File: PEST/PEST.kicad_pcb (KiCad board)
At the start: 4 copper layers, 6.2 x 4.9 mm, 4 parts, among them J1 Conn_01x01, J2 Conn_01x01, J3 Conn_01x01, J4 Conn_01x01

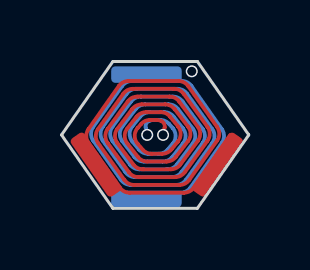
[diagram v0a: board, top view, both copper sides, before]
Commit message: Moved all pads to bottom layer
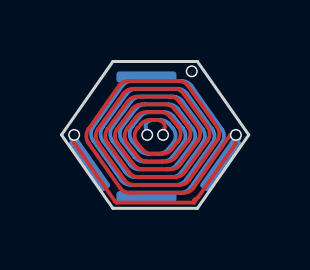
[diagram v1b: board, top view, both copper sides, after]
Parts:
- J1, J3: moved to B.Cu
- moved J3 0.22 mm to (17.8, 21.0)
- moved J1 0.11 mm to (22.2, 21.0)
- moved J2 0.08 mm to (19.7, 22.1)
- moved J4 0.08 mm to (19.7, 18.1)
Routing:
- net Net-(J1-Pin_1): track 195.2 -> 205.9 mm, vias 3 -> 5
